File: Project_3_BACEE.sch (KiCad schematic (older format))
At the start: 0 parts

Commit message: Created new child sheet, added project symbols.
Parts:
- added BT?: Battery, symbol Device:Battery
- added C? (x2): C, symbol Device:C
- added C?: CP, symbol Device:CP
- added D?: LED, symbol Device:LED
- added J?: Conn_01x09, symbol Connector_Generic:Conn_01x09
- added J? (x2): Conn_01x04, symbol Connector_Generic:Conn_01x04
- added J?: Conn_02x03_Odd_Even, symbol Connector_Generic:Conn_02x03_Odd_Even
- added R? (x2): R, symbol Device:R
- added U?: 24LC1025, symbol Memory_EEPROM:24LC1025
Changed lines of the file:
@@
 EESchema Schematic File Version 4
+LIBS:Project_3_BACEE-cache
 EELAYER 30 0
 EELAYER END
 $Descr A4 11693 8268
 encoding utf-8
-Sheet 1 1
+Sheet 1 2
 Title "BACEE_v1.0"
 Date "2019-09-19"
@@
 Comment4 ""
 $EndDescr
+$Comp
+L Device:Battery BT?
+U 1 1 5D8368FA
+P 3700 2550
+F 0 "BT?" H 3808 2596 50  0000 L CNN
+F 1 "Battery" H 3808 2505 50  0000 L CNN
+F 2 "" V 3700 2610 50  0001 C CNN
+F 3 "~" V 3700 2610 50  0001 C CNN
+	1    3700 2550
+	1    0    0    -1
+$EndComp
+$Comp
+L Device:C C?
+U 1 1 5D837139
+P 4500 2200
+F 0 "C?" H 4615 2246 50  0000 L CNN
+F 1 "C" H 4615 2155 50  0000 L CNN
+F 2 "" H 4538 2050 50  0001 C CNN
+F 3 "~" H 4500 2200 50  0001 C CNN
+	1    4500 2200
+	1    0    0    -1
+$EndComp
+$Comp
+L Device:C C?
+U 1 1 5D837758
+P 4500 2600
+F 0 "C?" H 4615 2646 50  0000 L CNN
+F 1 "C" H 4615 2555 50  0000 L CNN
+F 2 "" H 4538 2450 50  0001 C CNN
+F 3 "~" H 4500 2600 50  0001 C CNN
+	1    4500 2600
+	1    0    0    -1
+$EndComp
+$Comp
+L Device:CP C?
+U 1 1 5D837C3D
+P 5000 2200
+F 0 "C?" H 5118 2246 50  0000 L CNN
+F 1 "CP" H 5118 2155 50  0000 L CNN
+F 2 "" H 5038 2050 50  0001 C CNN
+F 3 "~" H 5000 2200 50  0001 C CNN
+	1    5000 2200
+	1    0    0    -1
+$EndComp
+$Comp
+L Device:LED D?
+U 1 1 5D8380C0
+P 3700 3100
+F 0 "D?" V 3739 2983 50  0000 R CNN
+F 1 "LED" V 3648 2983 50  0000 R CNN
+F 2 "" H 3700 3100 50  0001 C CNN
+F 3 "~" H 3700 3100 50  0001 C CNN
+	1    3700 3100
+	0    -1   -1   0
+$EndComp
+$Comp
+L Device:R R?
+U 1 1 5D8396B9
+P 5550 2200
+F 0 "R?" H 5620 2246 50  0000 L CNN
+F 1 "R" H 5620 2155 50  0000 L CNN
+F 2 "" V 5480 2200 50  0001 C CNN
+F 3 "~" H 5550 2200 50  0001 C CNN
+	1    5550 2200
+	1    0    0    -1
+$EndComp
+$Comp
+L Device:R R?
+U 1 1 5D839B71
+P 5550 2750
+F 0 "R?" H 5620 2796 50  0000 L CNN
+F 1 "R" H 5620 2705 50  0000 L CNN
+F 2 "" V 5480 2750 50  0001 C CNN
+F 3 "~" H 5550 2750 50  0001 C CNN
+	1    5550 2750
+	1    0    0    -1
+$EndComp
+$Comp
+L Memory_EEPROM:24LC1025 U?
+U 1 1 5D83A291
+P 6400 2250
+F 0 "U?" H 6400 2731 50  0000 C CNN
+F 1 "24LC1025" H 6400 2640 50  0000 C CNN
+F 2 "" H 6400 2250 50  0001 C CNN
+F 3 "http://ww1.microchip.com/downloads/en/DeviceDoc/21941B.pdf" H 6400 2250 50  0001 C CNN
+	1    6400 2250
+	1    0    0    -1
+$EndComp
+$Sheet
+S 5950 3550 2400 2150
+U 5D83B0D5
+F0 "Connectors" 50
+F1 "Connectors.sch" 50
+$EndSheet
+$Comp
+L Connector_Generic:Conn_01x09 J?
+U 1 1 5D83BD36
+P 4700 4900
+F 0 "J?" H 4780 4942 50  0000 L CNN
+F 1 "Conn_01x09" H 4780 4851 50  0000 L CNN
+F 2 "" H 4700 4900 50  0001 C CNN
+F 3 "~" H 4700 4900 50  0001 C CNN
+	1    4700 4900
+	1    0    0    -1
+$EndComp
+$Comp
+L Connector_Generic:Conn_01x04 J?
+U 1 1 5D83CD16
+P 5650 4800
+F 0 "J?" H 5730 4792 50  0000 L CNN
+F 1 "Conn_01x04" H 5730 4701 50  0000 L CNN
+F 2 "" H 5650 4800 50  0001 C CNN
+F 3 "~" H 5650 4800 50  0001 C CNN
+	1    5650 4800
+	1    0    0    -1
+$EndComp
+$Comp
+L Connector_Generic:Conn_02x03_Odd_Even J?
+U 1 1 5D83D5F4
+P 4800 6050
+F 0 "J?" H 4850 6367 50  0000 C CNN
+F 1 "Conn_02x03_Odd_Even" H 4850 6276 50  0000 C CNN
+F 2 "" H 4800 6050 50  0001 C CNN
+F 3 "~" H 4800 6050 50  0001 C CNN
+	1    4800 6050
+	1    0    0    -1
+$EndComp
+$Comp
+L Connector_Generic:Conn_01x04 J?
+U 1 1 5D83E499
+P 5700 5950
+F 0 "J?" H 5780 5942 50  0000 L CNN
+F 1 "Conn_01x04" H 5780 5851 50  0000 L CNN
+F 2 "" H 5700 5950 50  0001 C CNN
+F 3 "~" H 5700 5950 50  0001 C CNN
+	1    5700 5950
+	1    0    0    -1
+$EndComp
 $EndSCHEMATC

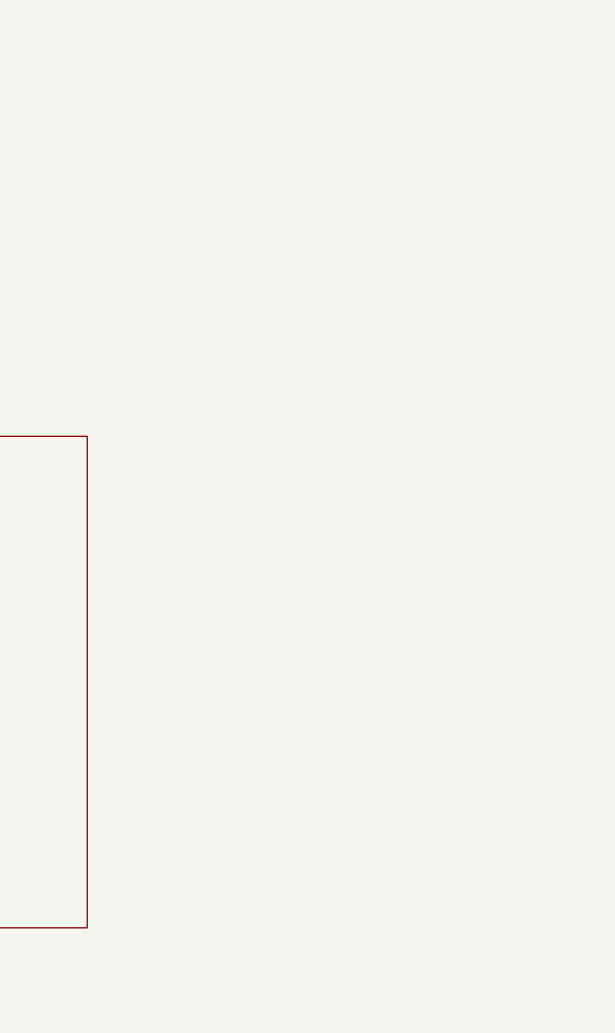
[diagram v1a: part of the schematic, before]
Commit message: Added symbol for Atmega328p-au.
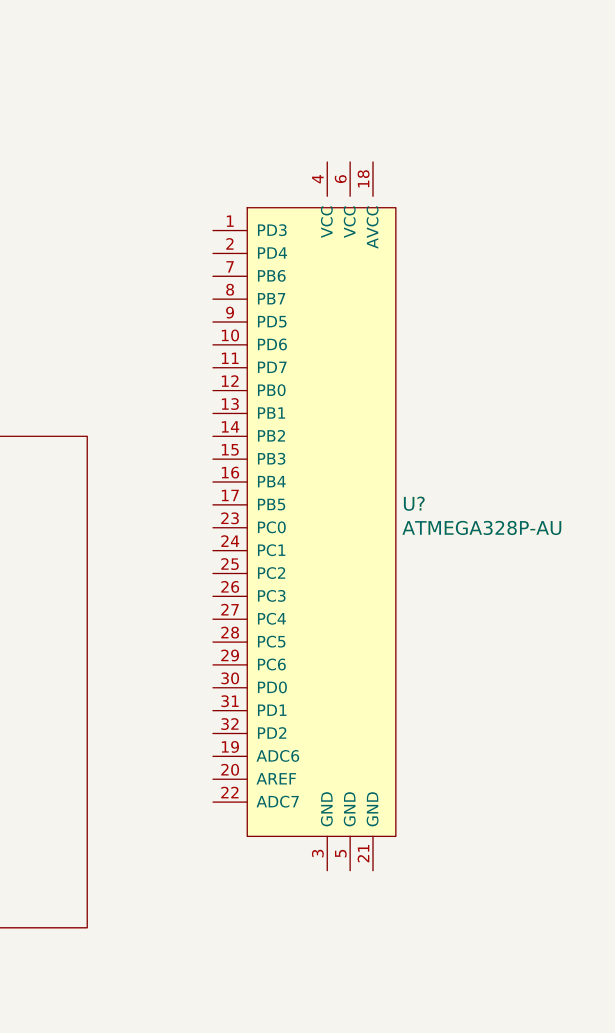
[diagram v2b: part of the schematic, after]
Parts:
- added U?: ATMEGA328P-AU, digikey-footprints:TQFP-32_7x7mm, symbol dk_Embedded-Microcontrollers:ATMEGA328P-AU
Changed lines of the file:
@@
+	1    0    0    -1
+$EndComp
+$Comp
+L dk_Embedded-Microcontrollers:ATMEGA328P-AU U?
+U 1 1 5D839D67
+P 9400 3950
+F 0 "U?" H 9728 4053 60  0000 L CNN
+F 1 "ATMEGA328P-AU" H 9728 3947 60  0000 L CNN
+F 2 "digikey-footprints:TQFP-32_7x7mm" H 9600 4150 60  0001 L CNN
+F 3 "http://www.microchip.com/mymicrochip/filehandler.aspx?ddocname=en608326" H 9600 4250 60  0001 L CNN
+F 4 "ATMEGA328P-AU-ND" H 9600 4350 60  0001 L CNN "Digi-Key_PN"
+F 5 "ATMEGA328P-AU" H 9600 4450 60  0001 L CNN "MPN"
+F 6 "Integrated Circuits (ICs)" H 9600 4550 60  0001 L CNN "Category"
+F 7 "Embedded - Microcontrollers" H 9600 4650 60  0001 L CNN "Family"
+F 8 "http://www.microchip.com/mymicrochip/filehandler.aspx?ddocname=en608326" H 9600 4750 60  0001 L CNN "DK_Datasheet_Link"
+F 9 "/product-detail/en/microchip-technology/ATMEGA328P-AU/ATMEGA328P-AU-ND/1832260" H 9600 4850 60  0001 L CNN "DK_Detail_Page"
+F 10 "IC MCU 8BIT 32KB FLASH 32TQFP" H 9600 4950 60  0001 L CNN "Description"
+F 11 "Microchip Technology" H 9600 5050 60  0001 L CNN "Manufacturer"
+F 12 "Active" H 9600 5150 60  0001 L CNN "Status"
+	1    9400 3950
 	1    0    0    -1
 $EndComp

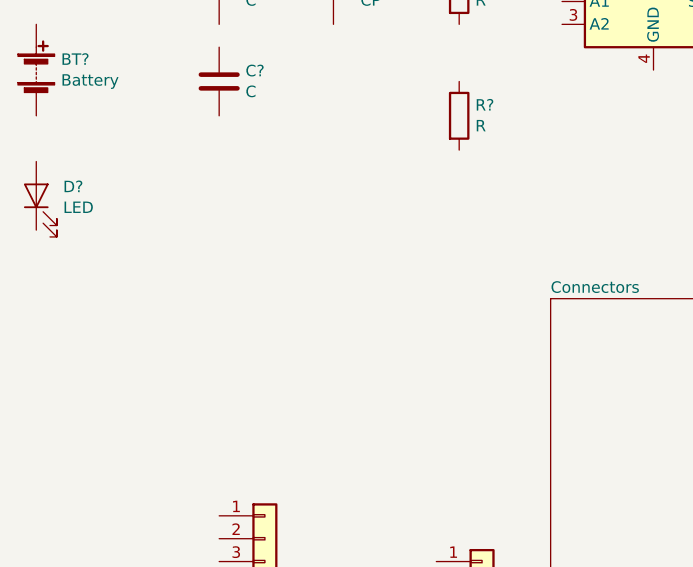
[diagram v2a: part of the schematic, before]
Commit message: Added costume DS1337 I2C Real Time Clock.
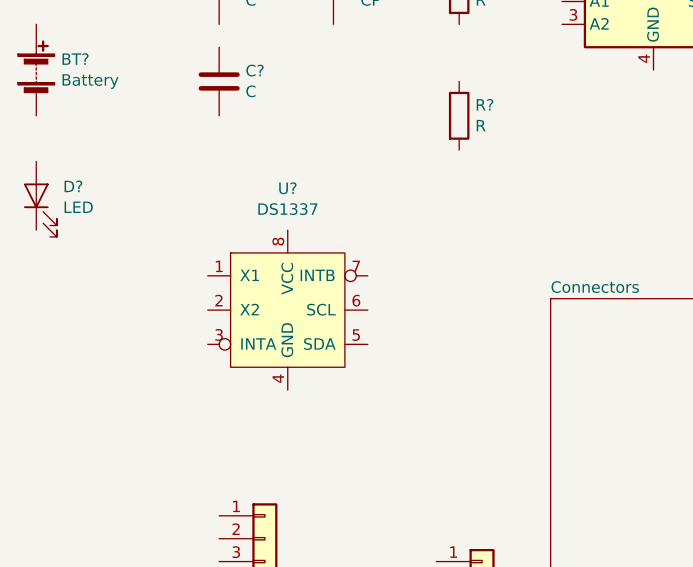
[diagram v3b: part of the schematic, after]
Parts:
- added U?: DS1337, symbol Real_Time_Clock:DS1337
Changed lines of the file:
@@
+	1    0    0    -1
+$EndComp
+$Comp
+L Real_Time_Clock:DS1337 U?
+U 1 1 5D83D55D
+P 4800 3600
+F 0 "U?" H 4800 4131 50  0000 C CNN
+F 1 "DS1337" H 4800 4040 50  0000 C CNN
+F 2 "" H 5050 4350 50  0001 C CNN
+F 3 "http://www.farnell.com/datasheets/2000844.pdf?_ga=2.177508589.917776798.1568905288-909876714.1550950510&_gac=1.216414692.1568905288.Cj0KCQjwzozsBRCNARIsAEM9kBOgoySVZbm8O6iFhnJvaEFTPgnKihPjdqZAtUZmWq1n3gbdbDGyVXUaAgFCEALw_wcB" H 5050 4350 50  0001 C CNN
+	1    4800 3600
 	1    0    0    -1
 $EndComp

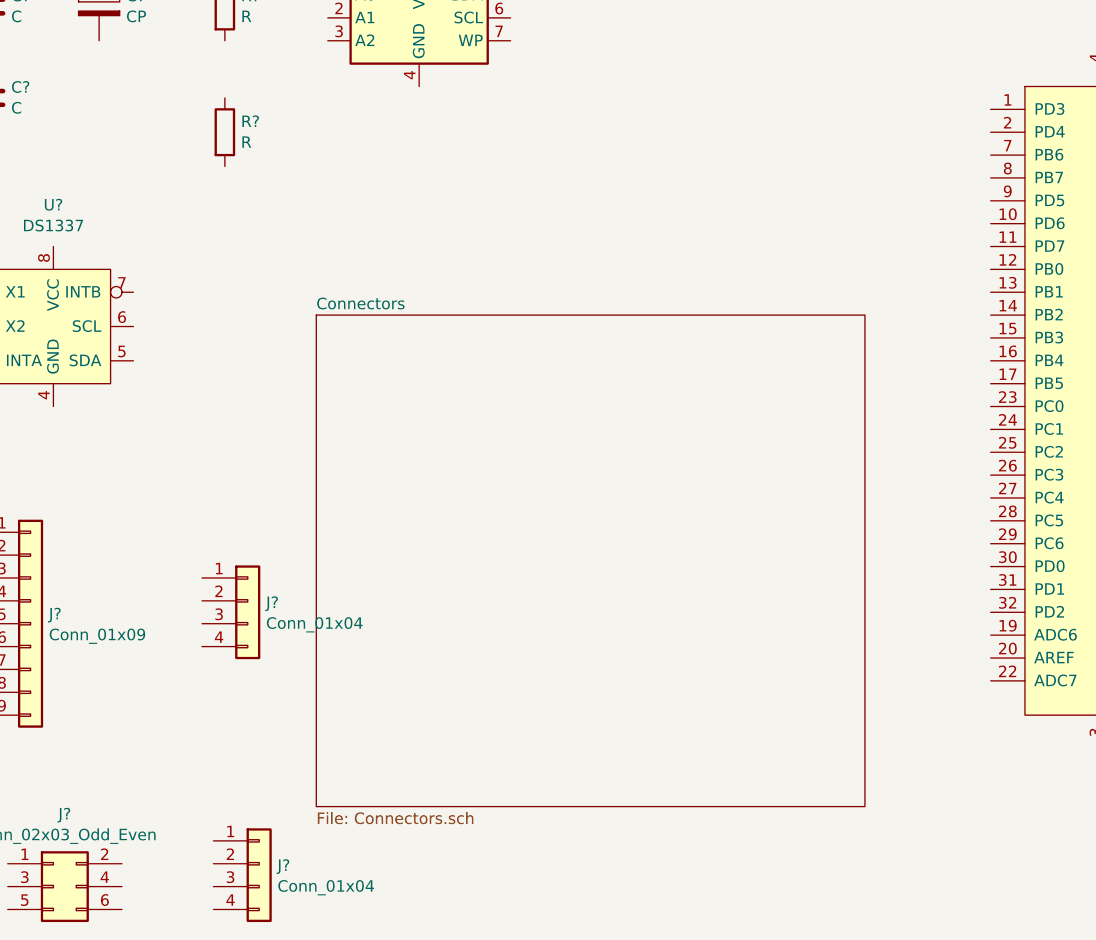
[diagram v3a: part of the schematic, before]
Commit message: Added missing crystals.
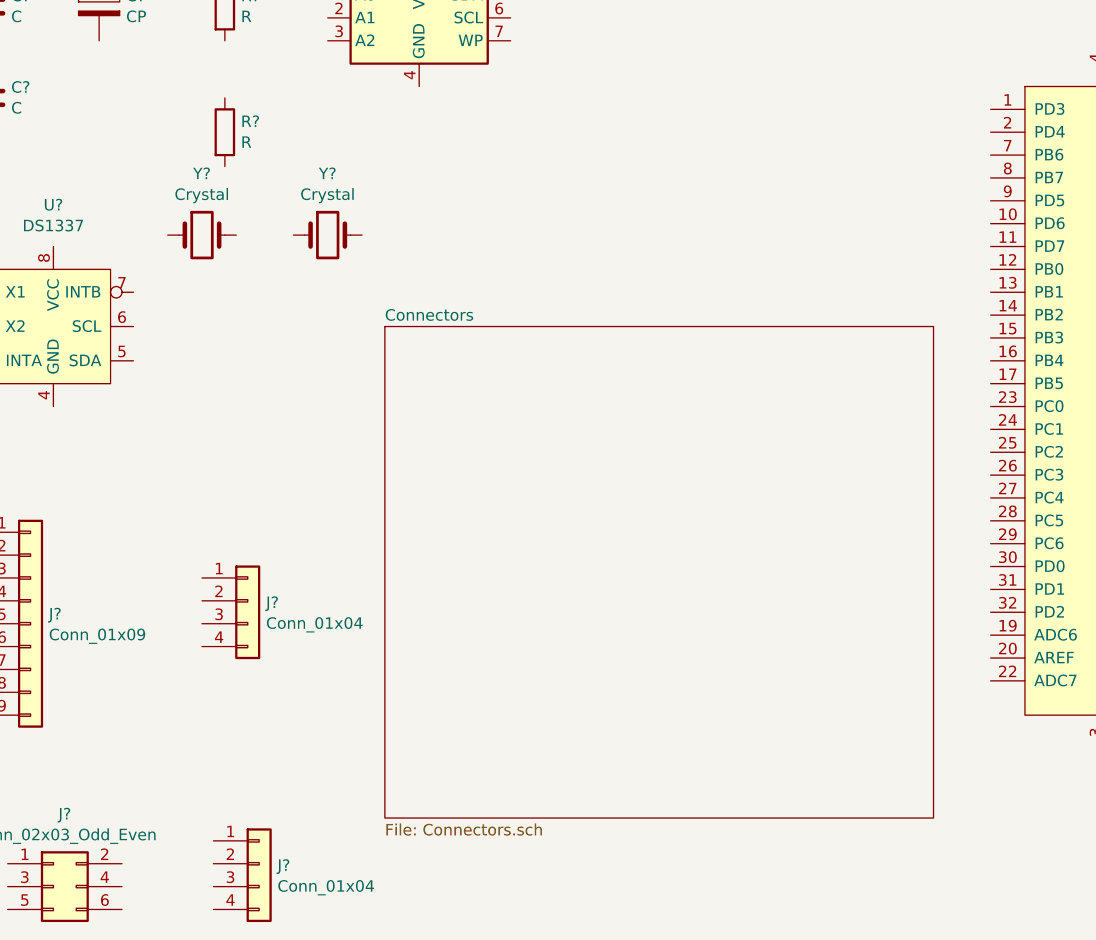
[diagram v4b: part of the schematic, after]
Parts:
- added Y? (x2): Crystal, symbol Device:Crystal
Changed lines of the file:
@@
 $EndComp
 $Sheet
-S 5950 3550 2400 2150
+S 6250 3600 2400 2150
 U 5D83B0D5
 F0 "Connectors" 50
@@
 	1    0    0    -1
 $EndComp
+$Comp
+L Device:Crystal Y?
+U 1 1 5D83E063
+P 5450 3200
+F 0 "Y?" H 5450 3468 50  0000 C CNN
+F 1 "Crystal" H 5450 3377 50  0000 C CNN
+F 2 "" H 5450 3200 50  0001 C CNN
+F 3 "~" H 5450 3200 50  0001 C CNN
+	1    5450 3200
+	1    0    0    -1
+$EndComp
+$Comp
+L Device:Crystal Y?
+U 1 1 5D83E859
+P 6000 3200
+F 0 "Y?" H 6000 3468 50  0000 C CNN
+F 1 "Crystal" H 6000 3377 50  0000 C CNN
+F 2 "" H 6000 3200 50  0001 C CNN
+F 3 "~" H 6000 3200 50  0001 C CNN
+	1    6000 3200
+	1    0    0    -1
+$EndComp
